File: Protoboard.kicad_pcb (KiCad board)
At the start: 2 copper layers, 135 x 105 mm, 56 parts, among them P1 CONN_01X08, P2 CONN_01X04, P3 CONN_01X05, P4 CONN_01X11, P5 CONN_02X05

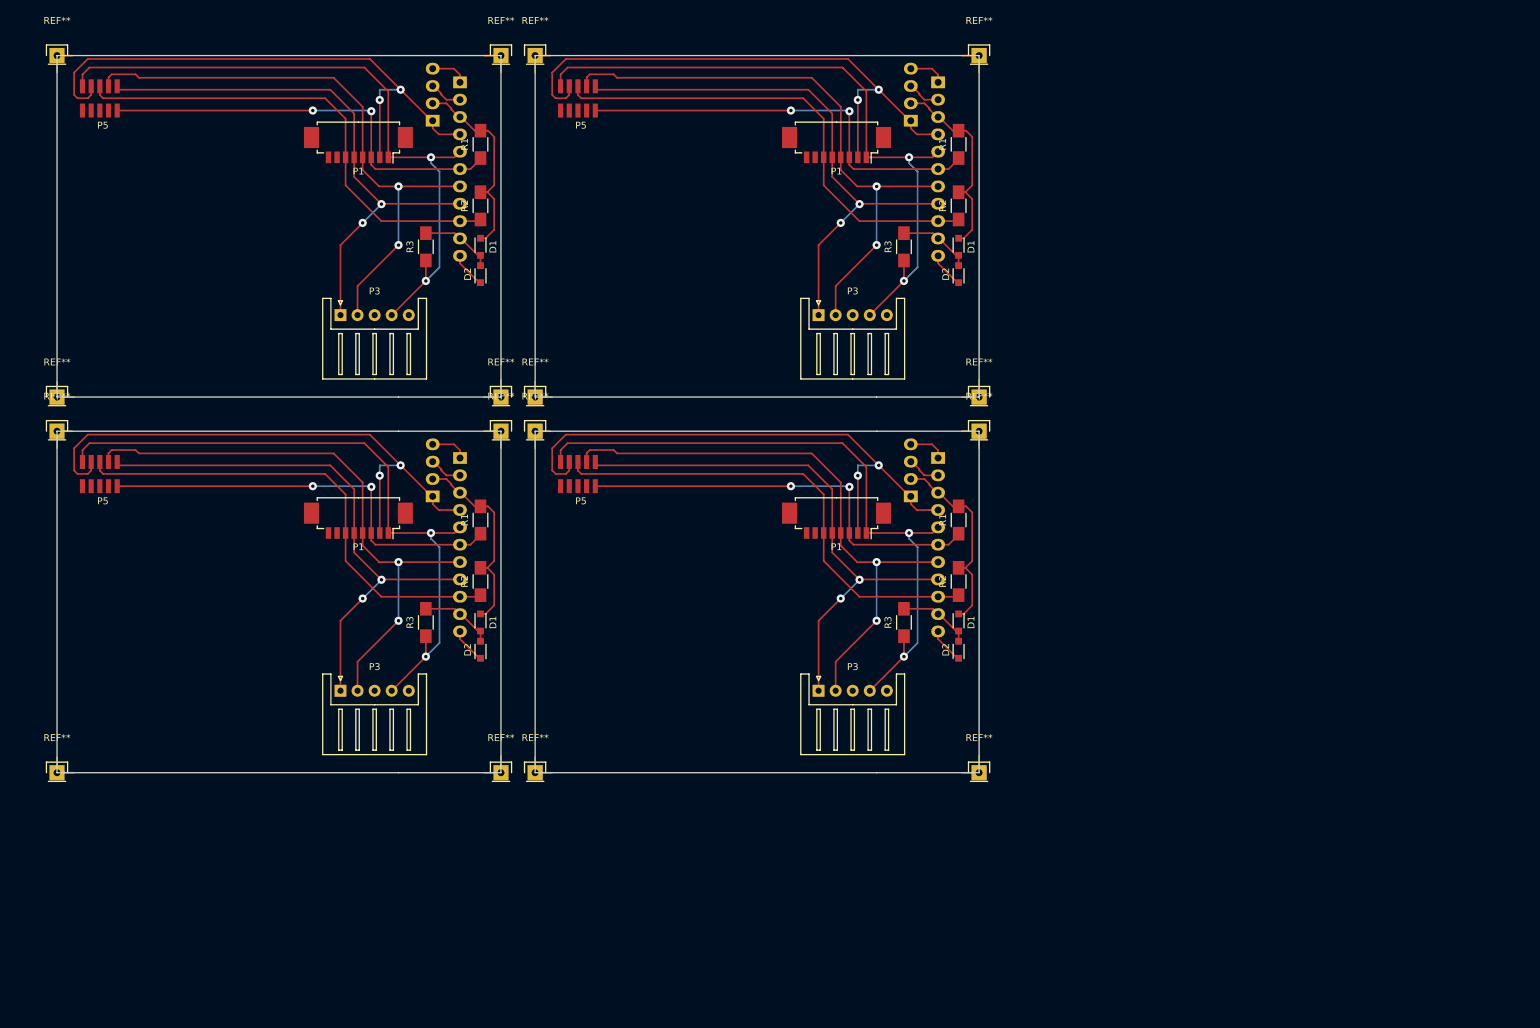
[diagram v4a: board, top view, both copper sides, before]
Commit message: Reorganized board, fixed bug with Molex Microblade connector (reversed pins).
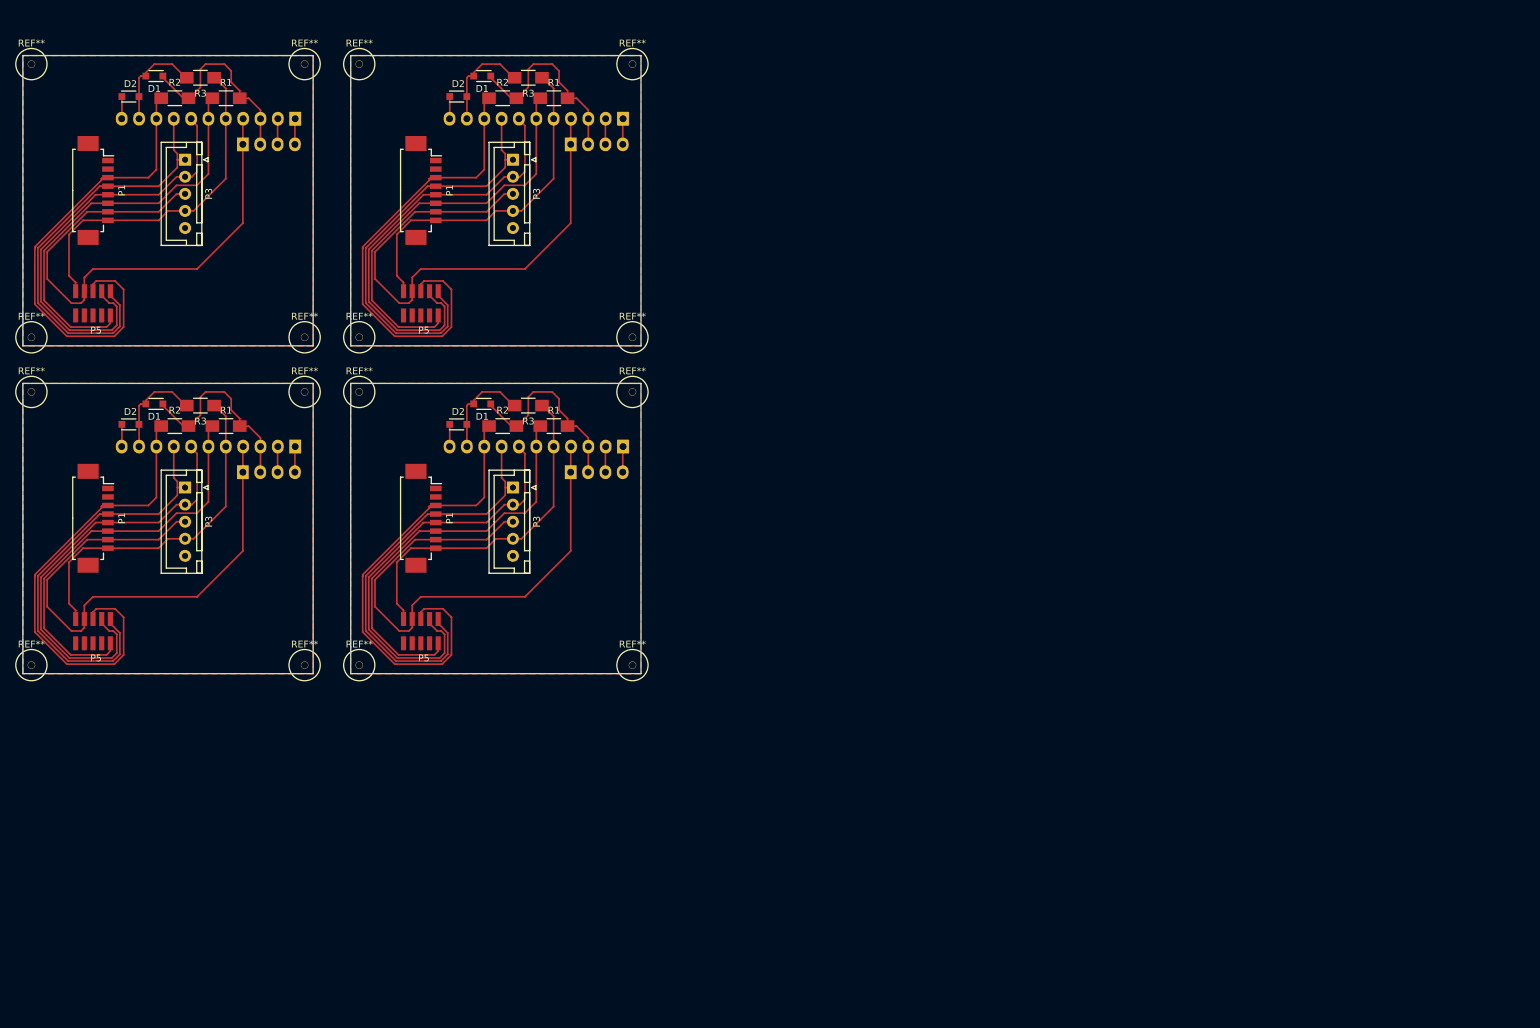
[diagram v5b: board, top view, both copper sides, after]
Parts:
- removed the D1 at (152.0, 103.0)
- removed the D1 at (152.0, 48.0)
- removed the D1 at (82.0, 103.0)
- removed the D2 at (152.0, 107.0)
- removed the D2 at (152.0, 52.0)
- removed the D2 at (82.0, 107.0)
- removed the P1 at (134.1, 88.5)
- removed the P1 at (134.1, 33.5)
- removed the P1 at (64.1, 88.5)
- removed the P2 at (145.0, 84.5)
- removed the P2 at (145.0, 29.5)
- removed the P2 at (75.0, 84.5)
- removed the P3 at (131.5, 113.0)
- removed the P3 at (131.5, 58.0)
- removed the P3 at (61.5, 113.0)
- removed the P3 at (61.5, 58.0)
- removed the P4 at (149.0, 78.9)
- removed the P4 at (149.0, 23.9)
- removed the P4 at (79.0, 78.9)
- removed the P5 at (93.7, 83.0)
- removed the P5 at (93.7, 28.1)
- removed the P5 at (23.7, 83.0)
- removed the R1 at (152.0, 88.0)
- removed the R1 at (152.0, 33.0)
- removed the R1 at (82.0, 88.0)
- removed the R2 at (152.0, 97.0)
- removed the R2 at (152.0, 42.0)
- removed the R2 at (82.0, 97.0)
- removed the R3 at (144.0, 103.0)
- removed the R3 at (144.0, 48.0)
- removed the R3 at (74.0, 103.0)
- removed the REF** at (90.0, 75.0)
- removed the REF** at (155.0, 125.0)
- removed the REF** at (155.0, 70.0)
- removed the REF** at (85.0, 125.0)
- removed the REF** at (20.0, 20.0)
- removed the REF** at (20.0, 70.0)
- removed the REF** at (85.0, 20.0)
- removed the REF** at (85.0, 70.0)
- removed the REF** at (90.0, 20.0)
- removed the REF** at (20.0, 75.0)
- removed the REF** at (90.0, 125.0)
- removed the REF** at (90.0, 70.0)
- removed the REF** at (20.0, 125.0)
- removed the REF** at (155.0, 75.0)
- removed the REF** at (155.0, 20.0)
- removed the REF** at (85.0, 75.0)
- added D1: D, Diodes_SMD:SOD-323_HandSoldering, F.Cu at (82.2, 71.0)
- added D1: D, Diodes_SMD:SOD-323_HandSoldering, F.Cu at (82.2, 23.0)
- added D1: D, Diodes_SMD:SOD-323_HandSoldering, F.Cu at (34.2, 71.0)
- added D2: D, Diodes_SMD:SOD-323_HandSoldering, F.Cu at (78.8, 74.0)
- added D2: D, Diodes_SMD:SOD-323_HandSoldering, F.Cu at (78.8, 26.0)
- added D2: D, Diodes_SMD:SOD-323_HandSoldering, F.Cu at (30.8, 74.0)
- added P1: CONN_01X08, Connectors_Molex:Molex_PicoBlade_53261-0871_08x1.25mm_Angled, F.Cu at (74.0, 87.8)
- added P1: CONN_01X08, Connectors_Molex:Molex_PicoBlade_53261-0871_08x1.25mm_Angled, F.Cu at (74.0, 39.8)
- added P1: CONN_01X08, Connectors_Molex:Molex_PicoBlade_53261-0871_08x1.25mm_Angled, F.Cu at (26.0, 87.8)
- added P2: CONN_01X04, Pin_Headers:Pin_Header_Straight_1x04, B.Cu at (95.2, 81.0)
- added P2: CONN_01X04, Pin_Headers:Pin_Header_Straight_1x04, B.Cu at (95.2, 33.0)
- added P2: CONN_01X04, Pin_Headers:Pin_Header_Straight_1x04, B.Cu at (47.2, 81.0)
- added P3: CONN_01X05, Connectors_JST:JST_XH_B05B-XH-A_05x2.50mm_Straight, F.Cu at (86.8, 83.2)
- added P3: CONN_01X05, Connectors_JST:JST_XH_B05B-XH-A_05x2.50mm_Straight, F.Cu at (86.8, 35.2)
- added P3: CONN_01X05, Connectors_JST:JST_XH_B05B-XH-A_05x2.50mm_Straight, F.Cu at (38.8, 83.2)
- added P3: CONN_01X05, Connectors_JST:JST_XH_B05B-XH-A_05x2.50mm_Straight, F.Cu at (38.8, 35.2)
- added P4: CONN_01X11, Pin_Headers:Pin_Header_Straight_1x11, B.Cu at (102.9, 77.2)
- added P4: CONN_01X11, Pin_Headers:Pin_Header_Straight_1x11, B.Cu at (102.9, 29.2)
- added P4: CONN_01X11, Pin_Headers:Pin_Header_Straight_1x11, B.Cu at (54.9, 77.2)
- added P5: CONN_02X05, Amphenol:Amphenol, F.Cu at (70.7, 106.0)
- added P5: CONN_02X05, Amphenol:Amphenol, F.Cu at (70.7, 58.0)
- added P5: CONN_02X05, Amphenol:Amphenol, F.Cu at (22.7, 106.0)
- added R1: 10k, Resistors_SMD:R_1206_HandSoldering, F.Cu at (92.8, 74.2)
- added R1: 10k, Resistors_SMD:R_1206_HandSoldering, F.Cu at (92.8, 26.2)
- added R1: 10k, Resistors_SMD:R_1206_HandSoldering, F.Cu at (44.8, 74.2)
- added R2: 10k, Resistors_SMD:R_1206_HandSoldering, F.Cu at (85.2, 74.2)
- added R2: 10k, Resistors_SMD:R_1206_HandSoldering, F.Cu at (85.2, 26.2)
- added R2: 10k, Resistors_SMD:R_1206_HandSoldering, F.Cu at (37.2, 74.2)
- added R3: 10k, Resistors_SMD:R_1206_HandSoldering, F.Cu at (89.0, 71.2)
- added R3: 10k, Resistors_SMD:R_1206_HandSoldering, F.Cu at (89.0, 23.2)
- added R3: 10k, Resistors_SMD:R_1206_HandSoldering, F.Cu at (41.0, 71.2)
- added REF**: 1pin, Connectors:1pin, F.Cu at (64.2, 69.2)
- added REF**: 1pin, Connectors:1pin, F.Cu at (64.2, 109.2)
- added REF**: 1pin, Connectors:1pin, F.Cu at (64.2, 61.2)
- added REF**: 1pin, Connectors:1pin, F.Cu at (16.2, 109.2)
- added REF**: 1pin, Connectors:1pin, F.Cu at (16.2, 61.2)
- added REF**: 1pin, Connectors:1pin, F.Cu at (56.2, 61.2)
- added REF**: 1pin, Connectors:1pin, F.Cu at (56.2, 21.2)
- added REF**: 1pin, Connectors:1pin, F.Cu at (16.2, 21.2)
- added REF**: 1pin, Connectors:1pin, F.Cu at (64.2, 21.2)
- added REF**: 1pin, Connectors:1pin, F.Cu at (16.2, 69.2)
- added REF**: 1pin, Connectors:1pin, F.Cu at (104.2, 69.2)
- added REF**: 1pin, Connectors:1pin, F.Cu at (104.2, 21.2)
- added REF**: 1pin, Connectors:1pin, F.Cu at (56.2, 69.2)
- added REF**: 1pin, Connectors:1pin, F.Cu at (104.2, 109.2)
- added REF**: 1pin, Connectors:1pin, F.Cu at (104.2, 61.2)
- added REF**: 1pin, Connectors:1pin, F.Cu at (56.2, 109.2)
- moved D2 57.5 mm to (30.8, 26.0), turned to 0 degrees
- moved D1 53.9 mm to (34.2, 23.0), turned to 180 degrees
- moved R2 47.4 mm to (37.2, 26.2), turned to 0 degrees
- moved R3 41.2 mm to (41.0, 23.2), turned to 180 degrees
- moved P1 38.6 mm to (26.0, 39.8), turned to 270 degrees
- moved R1 37.9 mm to (44.8, 26.2), turned to 0 degrees
- moved P5 30.0 mm to (22.7, 58.0)
- moved P2 28.0 mm to (47.2, 33.0), turned to 270 degrees
- moved P4 24.7 mm to (54.9, 29.2), turned to 90 degrees
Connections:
- P1 pad 1: +5V -> (no net)
- P1 pad 2: GND -> (no net)
- P1 pad 3: SET -> RESET
- P1 pad 4: RXD -> TXD
- P1 pad 5: TXD -> RXD
- P1 pad 6: RESET -> SET
- P1 pad 7: (no net) -> GND
- P1 pad 8: (no net) -> +5V
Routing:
- net +5V: track 393.5 -> 202.5 mm, vias 8 -> 0
- net RXD: track 345.9 -> 250.8 mm, vias 8 -> 0
- net (no net): track 78.0 -> 0.00 mm
- net TXD: track 326.6 -> 249.5 mm, vias 8 -> 0
- net DIN: track 43.4 -> 61.3 mm
- net GND: track 336.9 -> 324.6 mm, vias 8 -> 0
- net SET: track 248.5 -> 240.1 mm, vias 8 -> 0
- net LED: track 21.1 -> 13.0 mm
- net SCL: track 21.9 -> 15.1 mm
- net RESET: track 282.6 -> 276.0 mm
- net SDA: track 19.7 -> 15.1 mm
- net +3.3V: track 116.3 -> 115.4 mm
- added copper zone on F.Cu, net GND
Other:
- board size 135 x 105 mm -> 90.5 x 90.5 mm

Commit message: Improved track spacing for home brew UV etching.
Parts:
- added REF***: OSHW-Logo2_7.3x6mm_Copper, Symbols:OSHW-Logo2_7.3x6mm_Copper, F.Cu at (69.5, 73.8)
- added REF***: OSHW-Logo2_7.3x6mm_Copper, Symbols:OSHW-Logo2_7.3x6mm_Copper, F.Cu at (69.5, 25.8)
- added REF***: OSHW-Logo2_7.3x6mm_Copper, Symbols:OSHW-Logo2_7.3x6mm_Copper, F.Cu at (21.5, 73.8)
- added REF***: OSHW-Logo2_7.3x6mm_Copper, Symbols:OSHW-Logo2_7.3x6mm_Copper, F.Cu at (21.5, 25.8)
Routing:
- net RESET: track 276.0 -> 295.5 mm
- net TXD: track 249.5 -> 261.0 mm
- net GND: track 324.6 -> 318.1 mm
- net RXD: track 250.8 -> 255.7 mm
- net SET: track 240.1 -> 238.1 mm
- net +5V: track 202.5 -> 204.1 mm
